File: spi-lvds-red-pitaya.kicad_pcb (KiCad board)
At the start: 2 copper layers, 39.9 x 34.9 mm, 8 parts

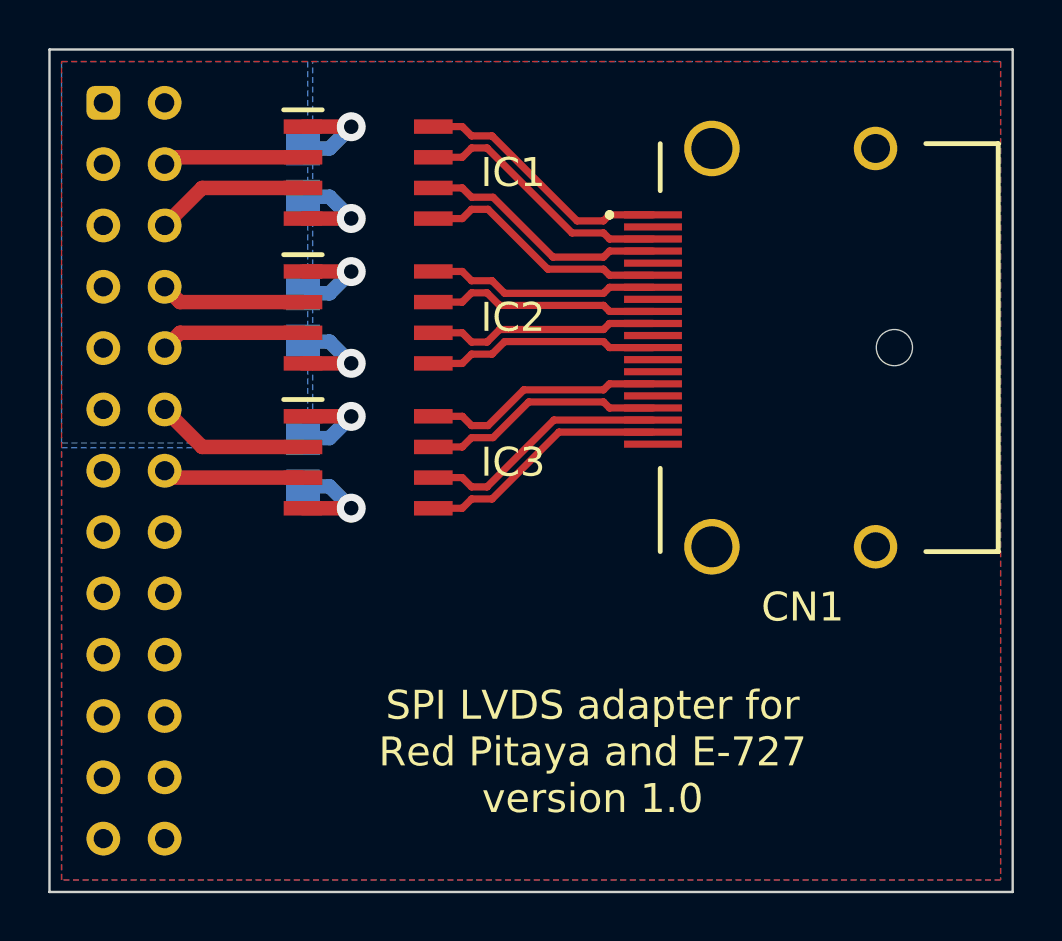
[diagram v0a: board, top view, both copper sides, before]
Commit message: update PCB for Red Pitaya
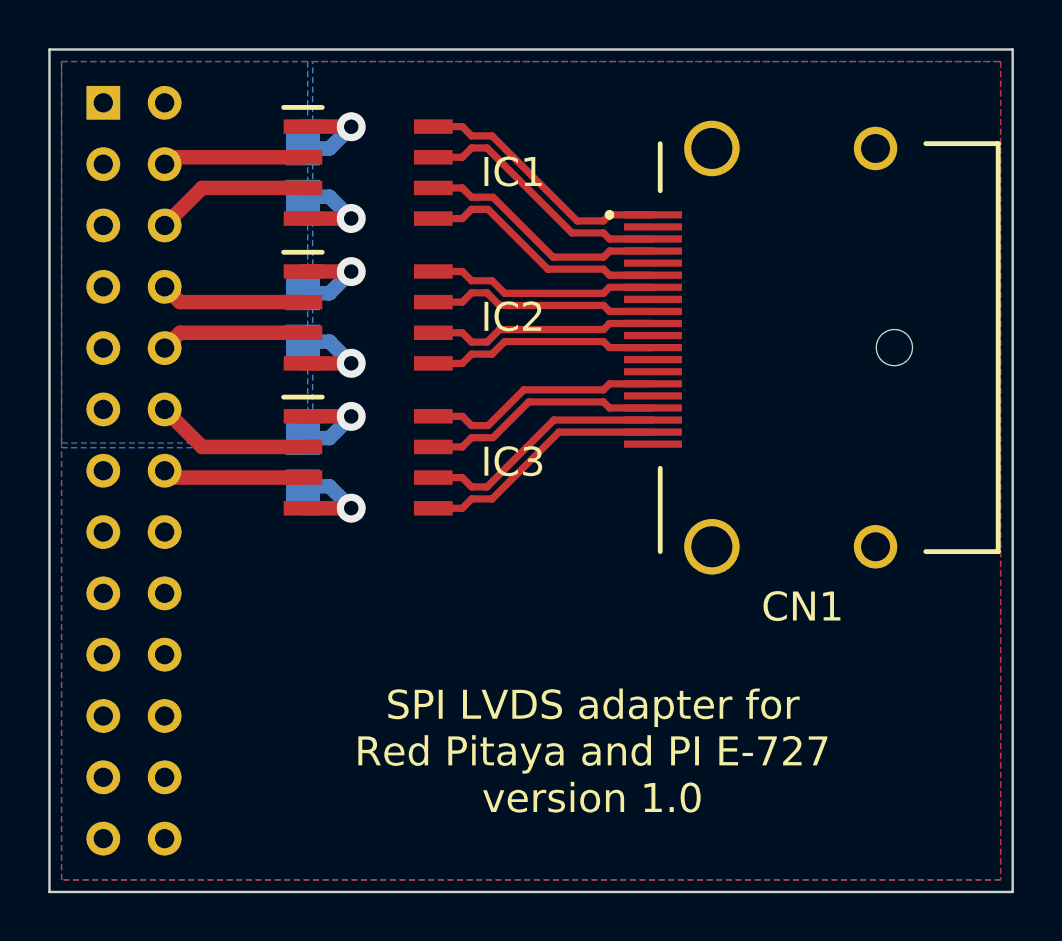
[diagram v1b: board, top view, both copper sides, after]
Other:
- board text added: "SPI LVDS adapter for Red Pitaya and PI E-727 version 1.0"
- board text removed: "SPI LVDS adapter for Red Pitaya and E-727 version 1.0"
